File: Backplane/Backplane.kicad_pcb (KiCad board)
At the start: 2 copper layers, 100 x 90.3 mm, 6 parts, among them J1 0, J2 0

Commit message: a bunch of stuff
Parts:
- removed S0: 0, 0-Footprints:Slot
- removed S1: 1, 0-Footprints:Slot
- removed S2: 2, 0-Footprints:Slot
- removed S3: 3, 0-Footprints:Slot
- added G1: Logo, 0-Footprints:Crank, F.Cu at (36.5, 73.9)
- added H1: ~, 0-Footprints:MountingHolePadM2.5, F.Cu at (27.6, 27.6)
- added H2: ~, 0-Footprints:MountingHolePadM2.5, F.Cu at (122.4, 27.6)
- added H3: ~, 0-Footprints:MountingHolePadM2.5, F.Cu at (27.6, 122.4)
- added H4: ~, 0-Footprints:MountingHolePadM2.5, F.Cu at (122.4, 122.4)
- added J3: Slot 2, 0-Footprints:Slot, F.Cu at (25.0, 92.8)
- added J4: Slot 3, 0-Footprints:Slot, F.Cu at (25.0, 79.3)
- added J5: Slot 4, 0-Footprints:Slot, F.Cu at (25.0, 65.8)
- added J6: Slot 5, 0-Footprints:Slot, F.Cu at (25.0, 52.3)
- added J7: Slot 6, 0-Footprints:Slot, F.Cu at (25.0, 38.8)
- added J8: Slot 7, 0-Footprints:Slot, F.Cu at (25.0, 25.3)
- added J9: Power, 0-Footprints:PinHeader_1x04_P2.54mm_Vertical, F.Cu at (40.2, 29.1)
- J1: value 0 -> Slot 0; footprint 0-Footprints:BusInterconnect-F -> 0-Footprints:Slot
- J2: value 0 -> Slot 1; footprint 0-Footprints:BusInterconnect-M -> 0-Footprints:Slot
- moved J1 94.8 mm to (25.0, 119.8)
- moved J2 0.16 mm to (25.0, 106.3)
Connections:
- net /RAM_BANK0 renamed /P28
- net /RAM_BANK1 renamed /P30
- net /S1 renamed /~{RAM_SEL}
- net /S10 renamed /P20
- net /S11 renamed /P22
- net /S12 renamed /P24
- net /S13 renamed /P26
- net /S2 renamed /~{ROM_SEL}
- net /S3 renamed /~{BANK_SEL}
- net /S4 renamed /~{IO_SEL}
- net /S5 renamed /P10
- net /S6 renamed /P12
- net /S7 renamed /P14
- net /S8 renamed /P16
- net /S9 renamed /P18
- J1 pad 32: /~{TSC} -> /P32
- J1 pad 33: /R/~{W} -> /BUS_OK
- J1 pad 34: /DBE -> /P34
- J1 pad 36: /~{HALT} -> /P36
- J1 pad 38: /~{IRQ} -> /P38
- J1 pad 40: /~{NMI} -> /P40
- J1 pad 42: /~{RESET} -> /P42
- J1 pad 44: /Φ1 -> /P44
- J1 pad 46: /Φ2 -> /R/~{W}
- J1 pad 48: /BA -> /~{IRQ}
- J1 pad 50: /VMA -> /~{RESET}
- J2 pad 32: /~{TSC} -> /P32
- J2 pad 33: /R/~{W} -> /BUS_OK
- J2 pad 34: /DBE -> /P34
- J2 pad 36: /~{HALT} -> /P36
- J2 pad 38: /~{IRQ} -> /P38
- J2 pad 40: /~{NMI} -> /P40
- J2 pad 42: /~{RESET} -> /P42
- J2 pad 44: /Φ1 -> /P44
- J2 pad 46: /Φ2 -> /R/~{W}
- J2 pad 48: /BA -> /~{IRQ}
- J2 pad 50: /VMA -> /~{RESET}
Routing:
- net /P18: track 0.00 -> 102.2 mm
- net /~{BANK_SEL}: track 0.00 -> 101.7 mm
- net /P14: track 0.00 -> 101.6 mm
- net /P24: track 0.00 -> 101.6 mm
- net /A0: track 0.00 -> 101.5 mm
- net /A12: track 0.00 -> 101.4 mm
- net /D5: track 0.00 -> 101.4 mm
- net /P16: track 0.00 -> 101.4 mm
- net /D2: track 0.00 -> 101.4 mm
- net /A10: track 0.00 -> 101.4 mm
- net /P28: track 0.00 -> 101.4 mm
- net /~{ROM_SEL}: track 0.00 -> 101.3 mm
- net /P22: track 0.00 -> 101.3 mm
- net /P44: track 0.00 -> 101.3 mm
- net /P26: track 0.00 -> 101.3 mm
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- added copper zone on F.Cu, net GND
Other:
- board size 100 x 90.3 mm -> 100 x 100 mm

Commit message: update the backplane
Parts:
- added G2: Logo, 0-Footprints:crankery_small, F.Cu at (36.1, 114.4)
- H1, H2, H3, H4: footprint 0-Footprints:MountingHolePadM2.5 -> 0-Footprints:MountingHole_3.2mm_M3
- J9: moved to B.Cu
- moved H4 0.34 mm to (122.2, 122.2)
- moved H2 0.34 mm to (122.2, 27.8)
- moved H3 0.34 mm to (27.8, 122.2)
- moved H1 0.34 mm to (27.8, 27.8)
- turned J9 to 90 degrees
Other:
- board text added: "C68BP.01"
- board text added: "JLCJLCJLCJLC"

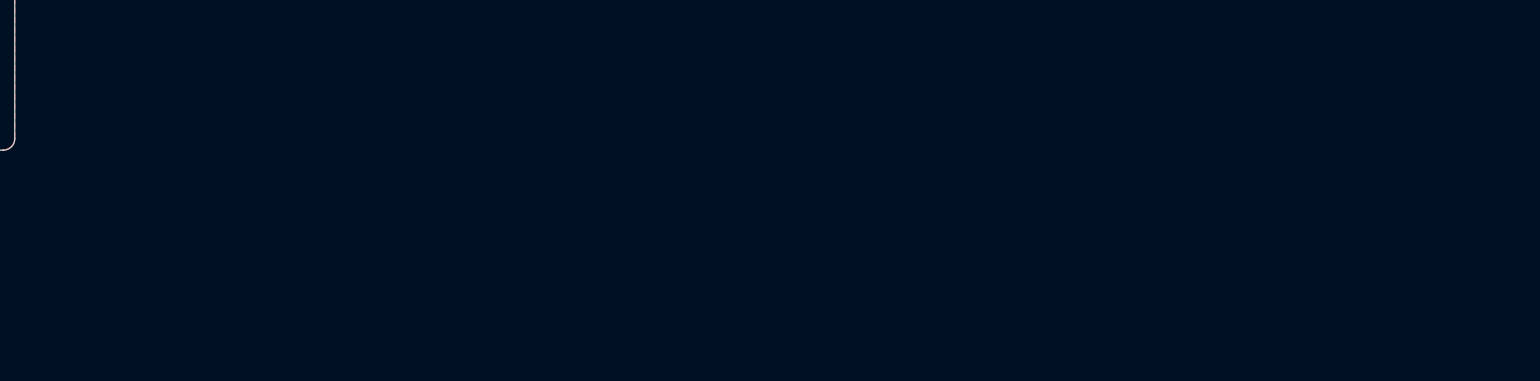
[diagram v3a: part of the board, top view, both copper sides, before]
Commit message: start moving things into folders for sanity's sake
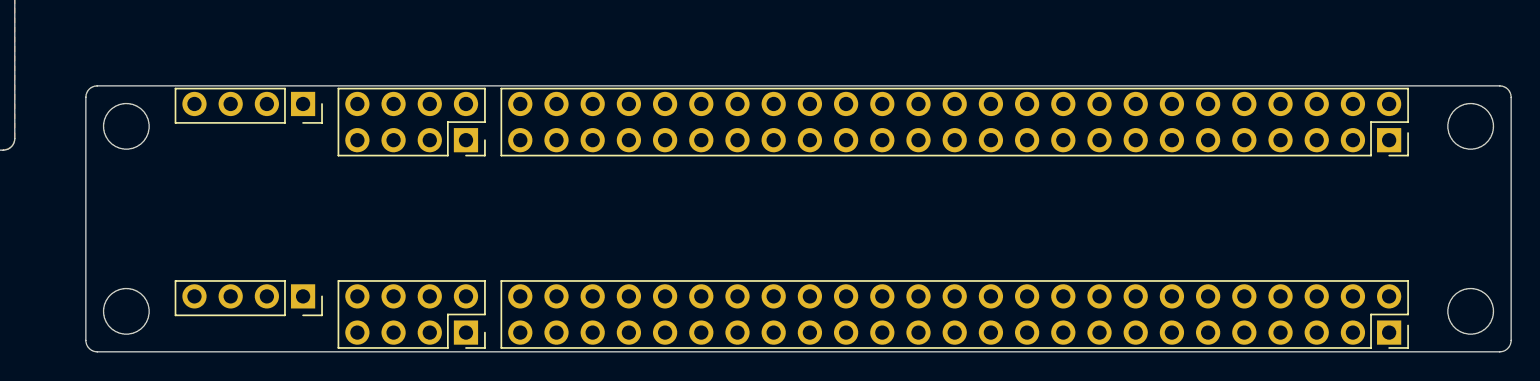
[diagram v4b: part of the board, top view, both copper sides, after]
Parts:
- added ?: , , F.Cu at (132.8, 123.3)
- added ?: , , F.Cu at (227.2, 123.3)
- added ?: , , F.Cu at (132.8, 136.3)
- added ?: , , F.Cu at (227.2, 136.3)
- added J1: Buss, 0-Footprints:Slot, F.Cu at (130.0, 120.5)
- added J2: Buss, 0-Footprints:Slot, F.Cu at (130.0, 134.0)
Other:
- board size 100 x 100 mm -> 205 x 114.2 mm

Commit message: lots of fixes to stack handling on emu, fix the latches on the banked memory board, tons of little bug fixes
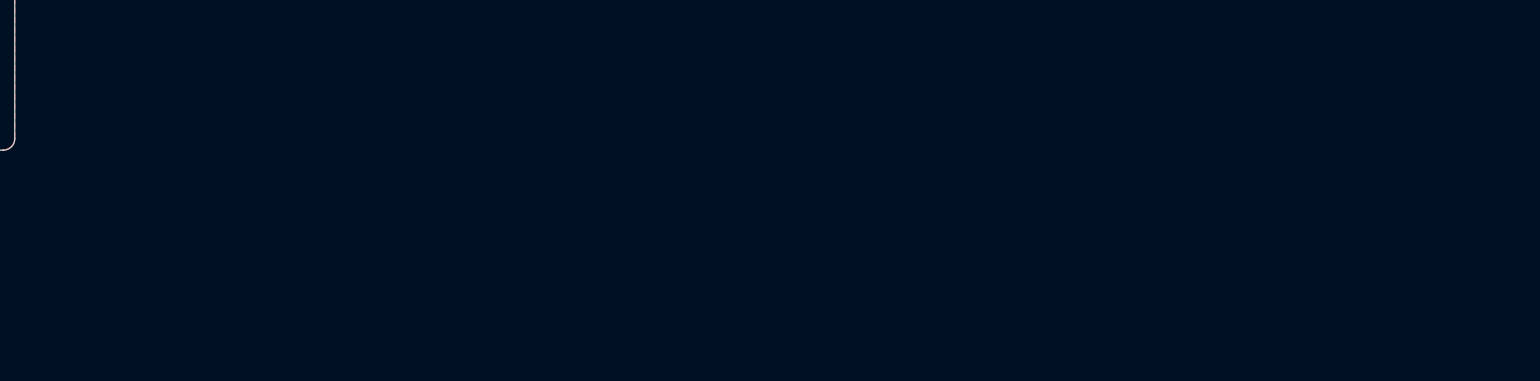
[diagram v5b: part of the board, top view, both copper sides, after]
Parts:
- removed ? (x4): , 
- removed the J1 at (130.0, 120.5)
- removed the J2 at (130.0, 134.0)
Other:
- board size 205 x 114.2 mm -> 100 x 100 mm
